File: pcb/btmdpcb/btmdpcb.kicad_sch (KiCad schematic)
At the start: 35 parts, among them J2 ANT, T1 ED8_4, T2 ED8_4, U2 Pololu_U1V11F3, U3 LMV331

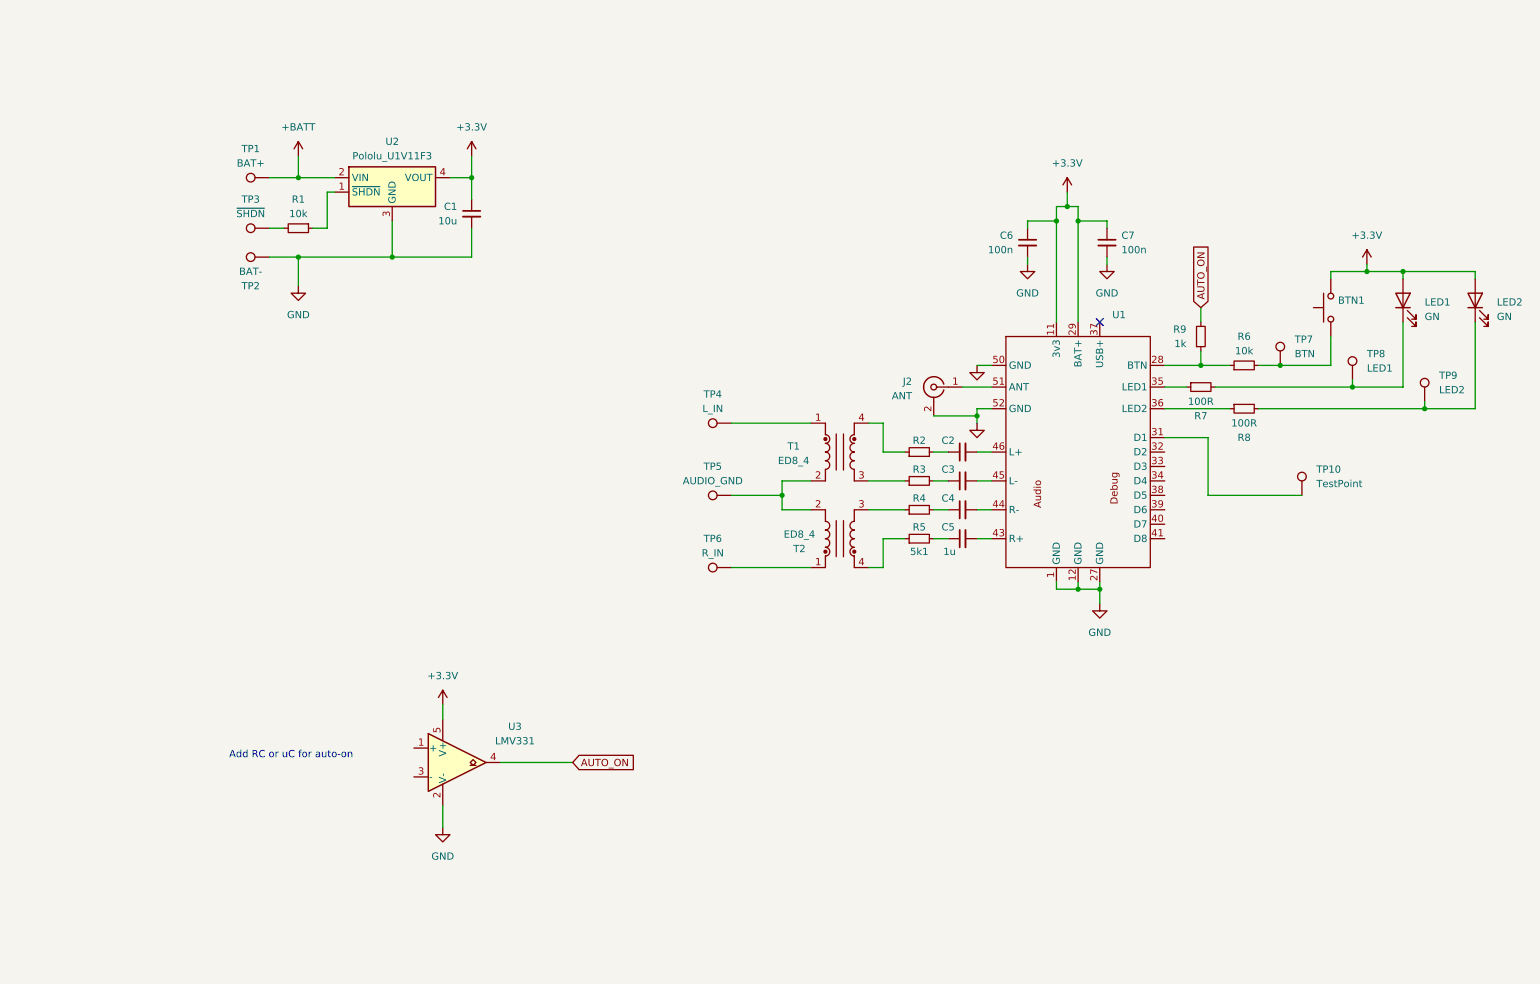
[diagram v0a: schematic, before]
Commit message: [WIP] Redo schematic for powering from 3.7V LiPo
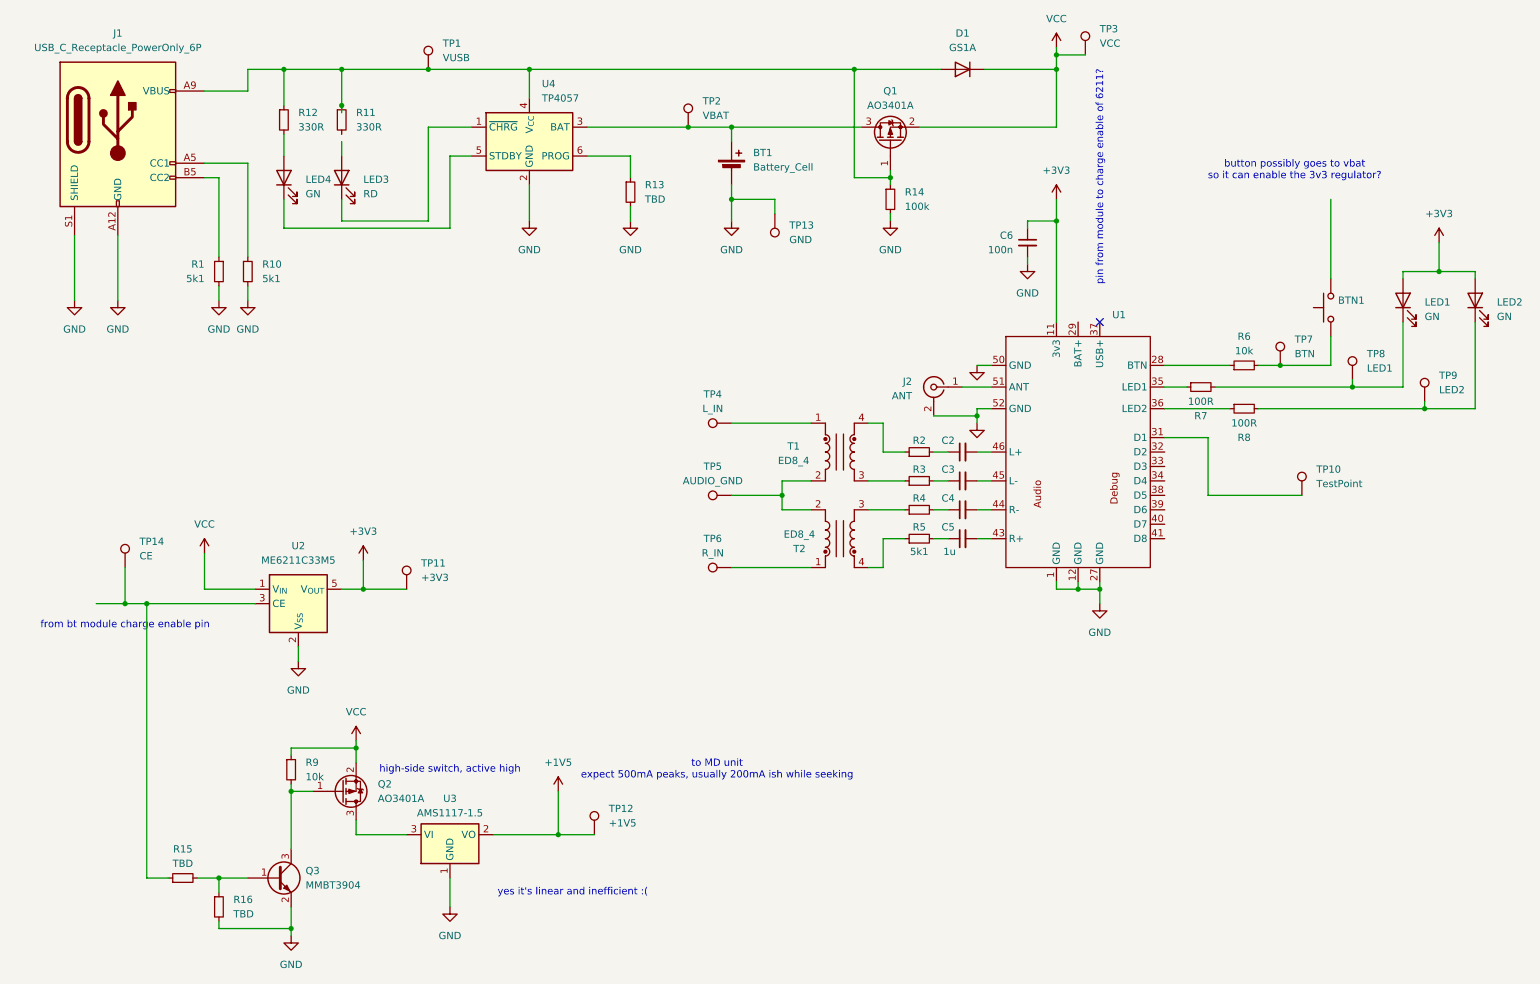
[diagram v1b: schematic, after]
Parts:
- removed C1: 10u, LED_SMD:LED_1206_3216Metric_Pad1.42x1.75mm_HandSolder, symbol Device:C_Small
- removed C7: 100n, Capacitor_SMD:C_0603_1608Metric_Pad1.08x0.95mm_HandSolder, symbol Device:C_Small
- removed U2: Pololu_U1V11F3, modules:Pololu_U1V11F3, symbol modules:Pololu_U1V11F3
- removed U3: LMV331, Package_TO_SOT_SMD:SOT-23-5_HandSoldering, symbol Comparator:LMV331
- added BT1: Battery_Cell, symbol Device:Battery_Cell
- added D1: GS1A, symbol Device:D
- added J1: USB_C_Receptacle_PowerOnly_6P, symbol Connector:USB_C_Receptacle_PowerOnly_6P
- added LED3: RD, LED_SMD:LED_0603_1608Metric_Pad1.05x0.95mm_HandSolder, symbol Device:LED
- added LED4: GN, LED_SMD:LED_0603_1608Metric_Pad1.05x0.95mm_HandSolder, symbol Device:LED
- added Q1, Q2: AO3401A, Package_TO_SOT_SMD:SOT-23, symbol Transistor_FET:AO3401A
- added Q3: MMBT3904, Package_TO_SOT_SMD:SOT-23, symbol Transistor_BJT:MMBT3904
- added R10: 5k1, symbol Device:R_Small
- added R11, R12: 330R, symbol Device:R_Small
- added R13, R15, R16: TBD, symbol Device:R_Small
- added R14: 100k, symbol Device:R_Small
- added TP11: +3V3, symbol Connector:TestPoint
- added TP12: +1V5, symbol Connector:TestPoint
- added TP13: GND, symbol Connector:TestPoint
- added TP14: CE, symbol Connector:TestPoint
- added U2: ME6211C33M5, Package_TO_SOT_SMD:SOT-23-5, symbol Regulator_Linear:ME6211C33M5
- added U3: AMS1117-1.5, Package_TO_SOT_SMD:SOT-223-3_TabPin2, symbol Regulator_Linear:AMS1117-1.5
- added U4: TP4057, Package_TO_SOT_SMD:TSOT-23-5, symbol Battery_Management:TP4057
- R1: value 10k -> 5k1; footprint Resistor_SMD:R_0603_1608Metric_Pad0.98x0.95mm_HandSolder -> (none)
- R9: value 1k -> 10k; footprint Resistor_SMD:R_0603_1608Metric_Pad0.98x0.95mm_HandSolder -> (none)
- TP1: value BAT+ -> VUSB; footprint TestPoint:TestPoint_Pad_D1.0mm -> (none)
- TP2: value BAT- -> VBAT; footprint TestPoint:TestPoint_Pad_D1.0mm -> (none)
- TP3: value ~{SHDN} -> VCC; footprint TestPoint:TestPoint_Pad_D1.0mm -> (none)
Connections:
- net GND: now also R1.2, BT1.2 (-), J1.A12 (GND), J1.B12 (GND), J1.S1 (SHIELD), Q3.2 (E), R10.2, R13.2, R14.2, R16.2, TP13.1, U2.2 (V_{SS}), U3.1 (GND), U4.2 (GND); no longer TP2.1
- net at R6.1, U1.28 (BTN): no longer R9.1
- net at R1.1: now also J1.B5 (CC2)
- net VCC: now reaches TP3.1
- net VCC: now also R9.1, D1.1 (K), Q1.2 (S), Q2.2 (S), U2.1 (V_{IN}); no longer R1.2
- net +3.3V renamed +3V3
- net +3V3: now also TP11.1, U2.5 (V_{OUT}); no longer BTN1.2, U1.29 (BAT+)
- net +BATT: no longer names the net of TP1.1
- net +BATT: now also D1.2 (A), J1.A9 (VBUS), J1.B9 (VBUS), Q1.1 (G), R11.1, R12.1, R14.1, U4.4 (V_{CC})
- net AUTO_ON: no longer names the net of R9.2
- net AUTO_ON: now also Q2.1 (G), Q3.3 (C)
- new net: R15.1, TP14.1, U2.3 (CE)
- new net: Q3.1 (B), R15.2, R16.1
- new net: LED4.1 (K), U4.5 (STDBY)
- new net: LED4.2 (A), R12.2
- new net: BT1.1 (+), Q1.3 (D), TP2.1, U4.3 (BAT)
- new net: LED3.1 (K), U4.1 (~{CHRG})
- new net: Q2.3 (D), U3.3 (VI)
- new net: J1.A5 (CC1), R10.1
- new net: R13.1, U4.6 (PROG)
- new net +1V5: TP12.1, U3.2 (VO)
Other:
- note added: "button possibly goes to vbat so it can enable the 3v3 regulator?"
- note added: "from bt module charge enable pin"
- note added: "high-side switch, active high"
- note added: "pin from module to charge enable of 6211?"
- note added: "to MD unit expect 500mA peaks, usually 200mA ish while seeking"
- note added: "yes it's linear and inefficient :("
- note removed: "Add RC or uC for auto-on"

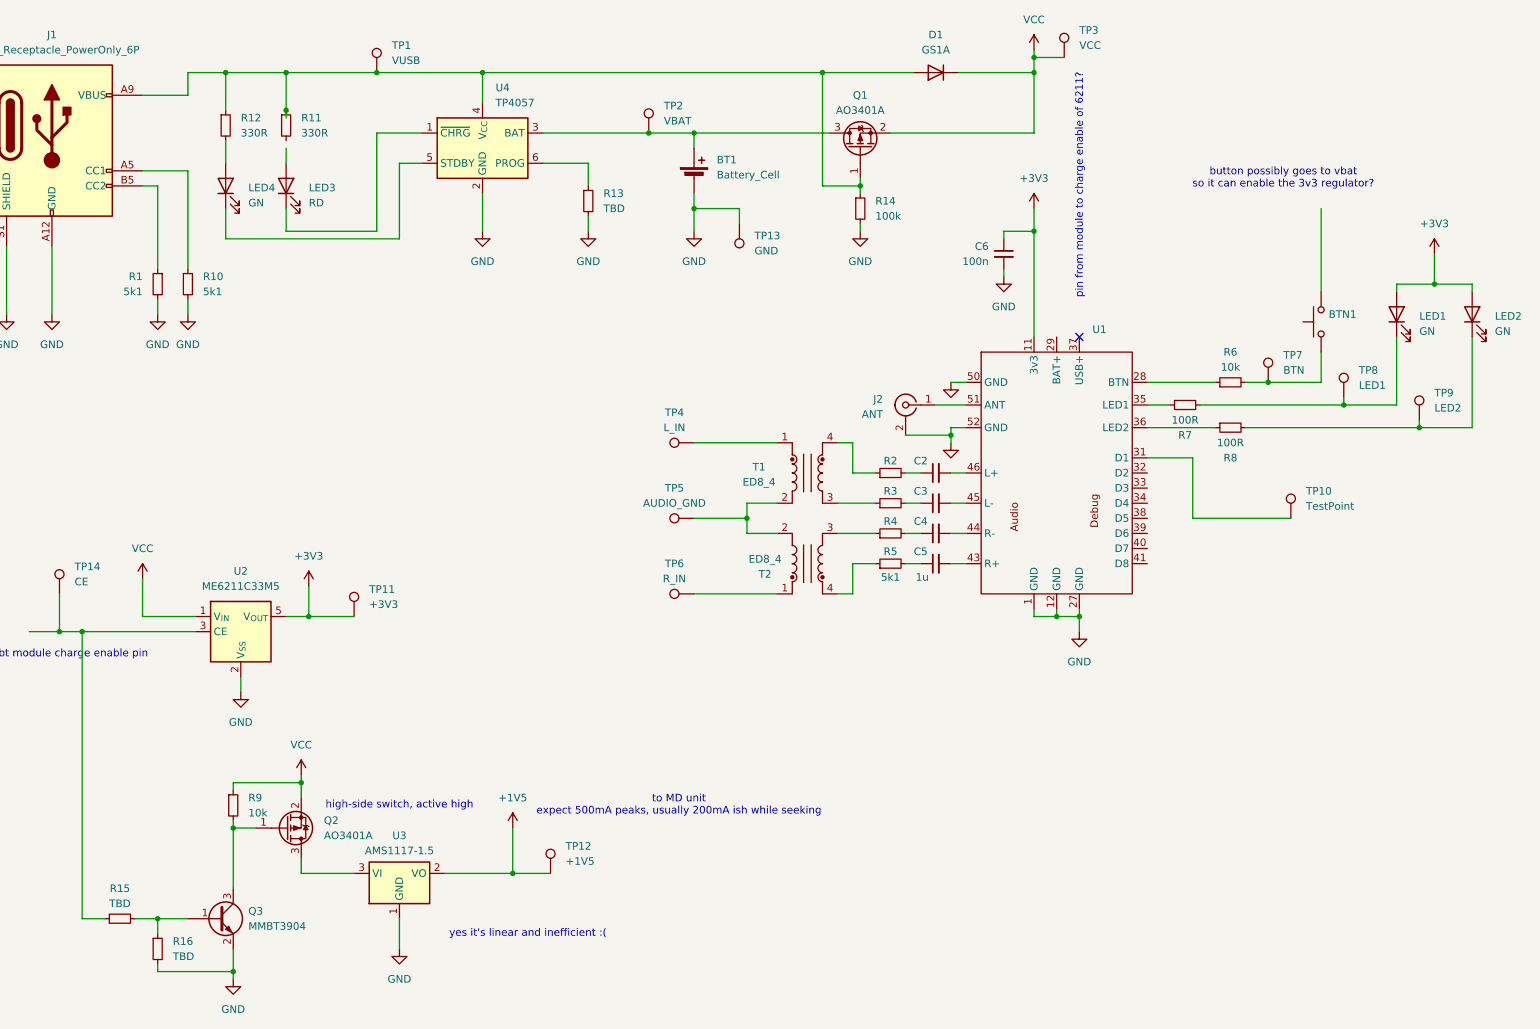
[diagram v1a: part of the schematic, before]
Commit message: Update BT module symbol+footprint (correct power labels, add CE)
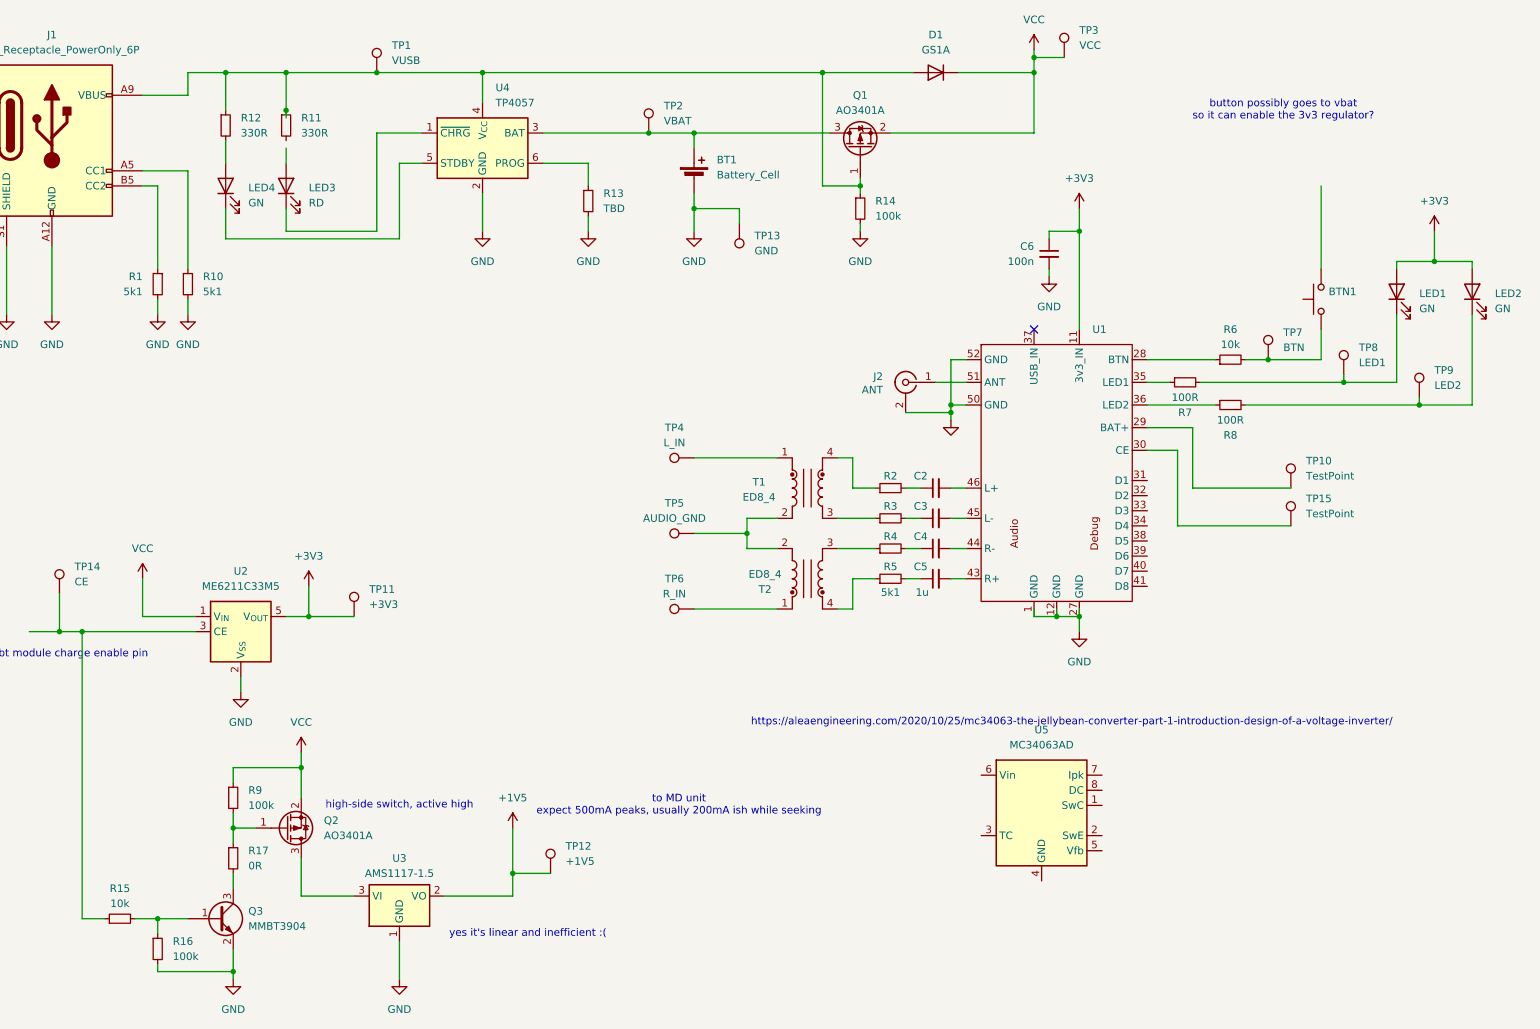
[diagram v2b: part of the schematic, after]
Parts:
- added R17: 0R, symbol Device:R_Small
- added TP15: TestPoint, TestPoint:TestPoint_Pad_D1.0mm, symbol Connector:TestPoint
- added U5: MC34063AD, Package_SO:SOIC-8_3.9x4.9mm_P1.27mm, symbol Regulator_Switching:MC34063AD
- R15: value TBD -> 10k
- R16: value TBD -> 100k
- R9: value 10k -> 100k
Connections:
- net at Q2.1 (G), R9.2: now also R17.1; no longer Q3.3 (C)
- net at U1.29 (BAT+): now also TP10.1
- net at U1.31 (D1): no longer TP10.1
- new net: Q3.3 (C), R17.2
- new net: TP15.1, U1.30 (CE)
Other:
- note added: "https://aleaengineering.com/2020/10/25/mc34063-the-jellybean-converter-part-1-introduction-design-of-a-voltage-inverter/"
- note removed: "pin from module to charge enable of 6211?"
- moved on the sheet: BTN1, C2, C3, C4, C5, C6, J2, LED1, LED2, R2, R3, R4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
